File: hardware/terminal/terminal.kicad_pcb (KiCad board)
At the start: 2 copper layers, 60 x 40 mm, 33 parts, among them IC1 ATMEGA8-P, J1 RJ45, P1 Prog, P10 CONN_4, P11 CONN_5X2, P12 CONN_4, P13 CONN_3X2, P14 CONN_5X2, P2 RC522, P3 LCD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

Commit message: o Add version 0.1 "reboot" o add some default trace widths.
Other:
- net class Default: trace_width 0.635 -> 0.3048
- net class thin removed
- board text added: ""Reboot""
- board text added: "v. 0.1"

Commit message: o connect 7 and 8 to 12V. o Better labelling RX/TX on board.
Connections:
- J1 pad 8: Net-(J1-Pad8) -> +12V
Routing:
- net +12V: track 37.5 -> 40.6 mm
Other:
- board text added: "<TX"
- board text added: ">RX"
- board text added: "RS232"
- board text added: "RX<"
- board text added: "TX>"
- board text removed: "RX"
- board text removed: "TX"

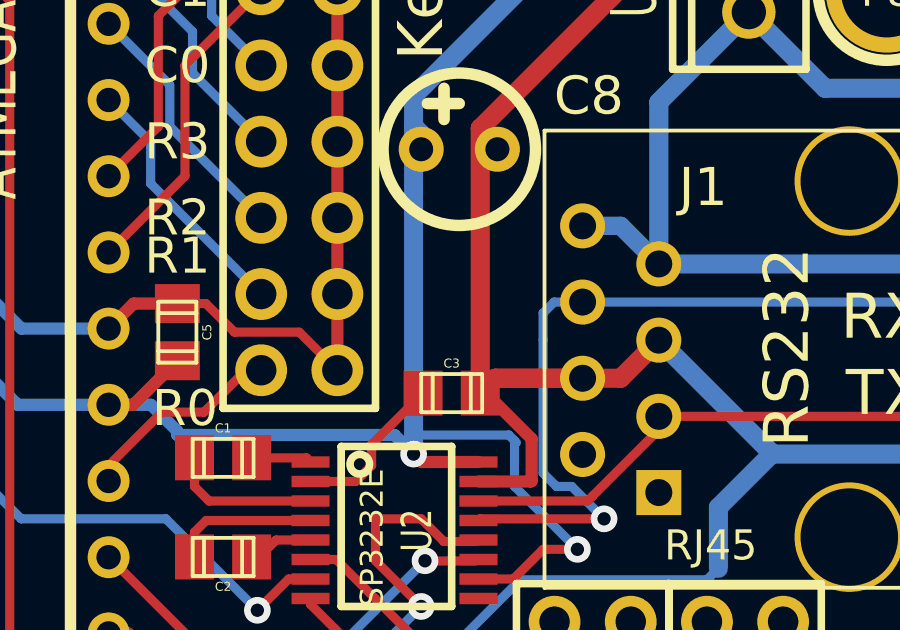
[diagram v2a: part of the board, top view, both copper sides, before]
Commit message: o anothe de-coupling capacitor close to the SP3232E can't harm.
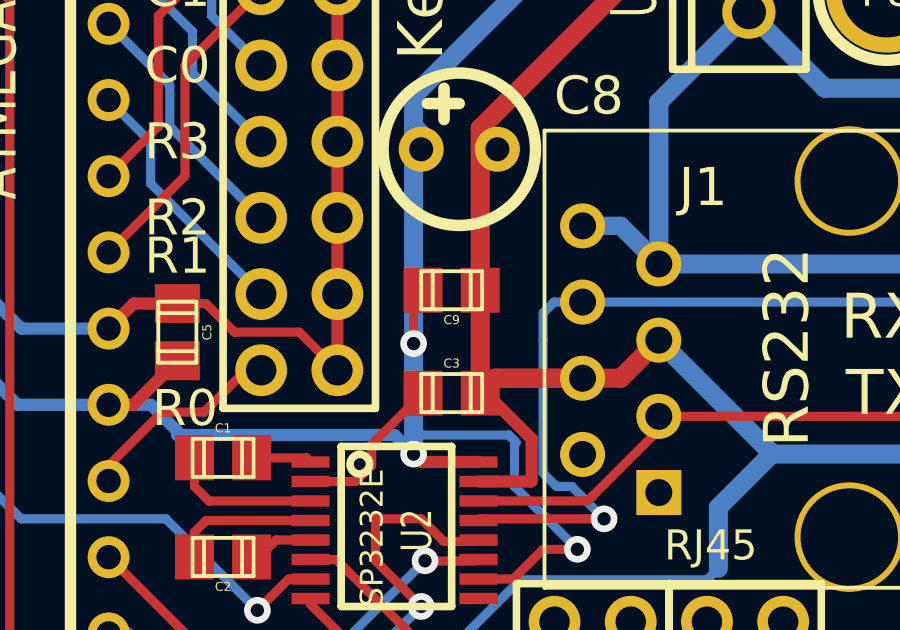
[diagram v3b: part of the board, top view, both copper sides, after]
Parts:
- added C9: C, Capacitors_SMD:c_0805, F.Cu at (158.5, 52.5)
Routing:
- net +3.3V: track 143.5 -> 145.4 mm, vias 4 -> 5
